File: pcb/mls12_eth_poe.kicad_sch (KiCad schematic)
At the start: 24 parts

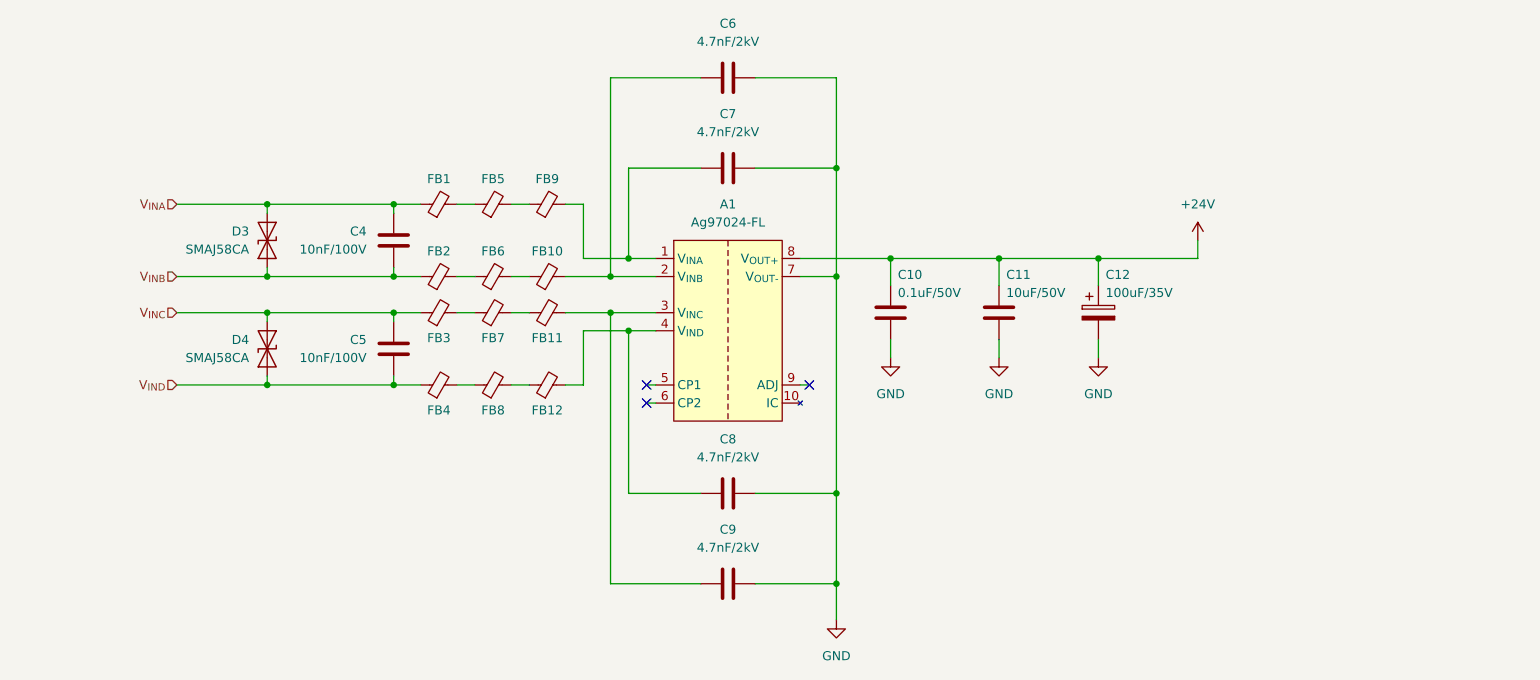
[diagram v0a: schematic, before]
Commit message: Update to 25W PoE+ module, 2 outputs
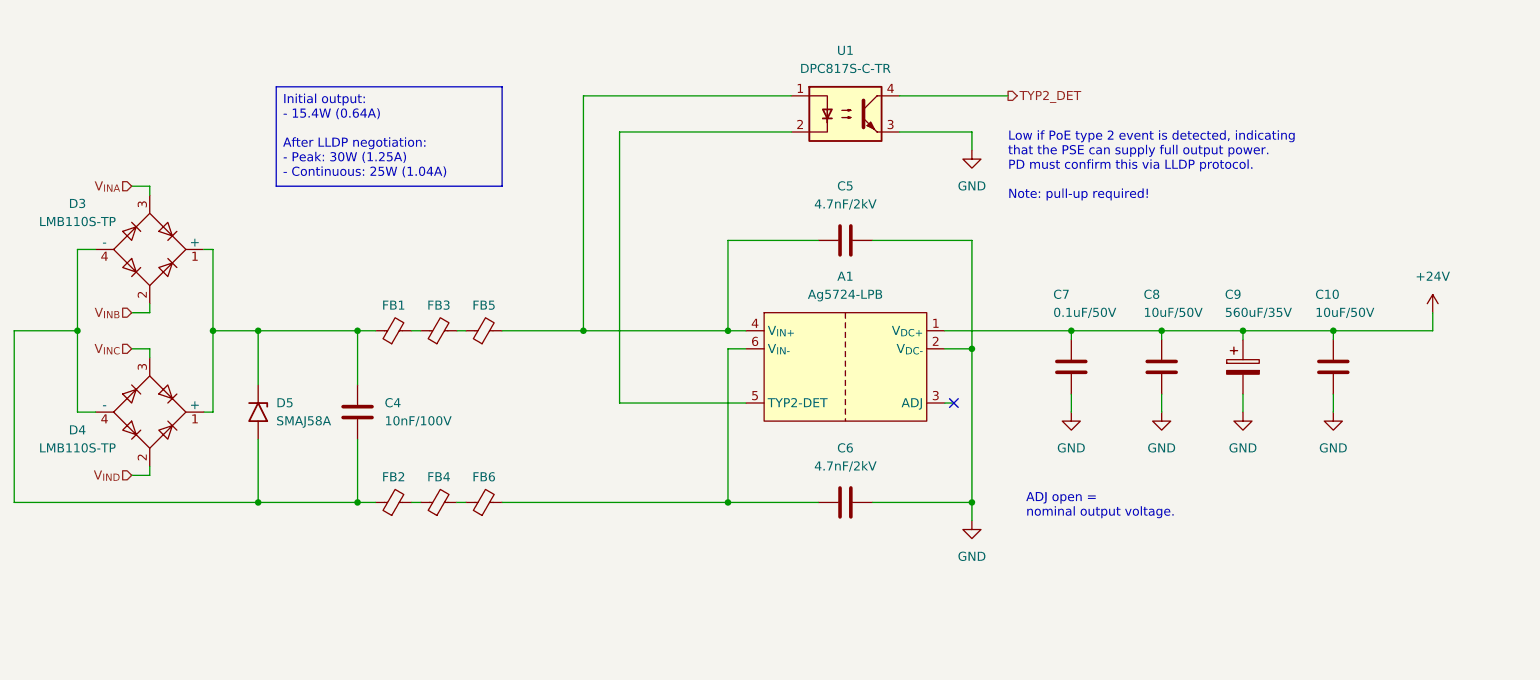
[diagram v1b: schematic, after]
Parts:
- removed A1: Ag97024-FL, mls12:Ag97024-FL, symbol mls12:Ag97024-FL
- removed C11: 10uF/50V, Capacitor_SMD:C_1206_3216Metric, symbol Device:C
- removed C12: 100uF/35V, Capacitor_SMD:CP_Elec_6.3x5.9, symbol Device:C_Polarized
- removed C9: 4.7nF/2kV, Capacitor_SMD:C_1210_3225Metric, symbol Device:C
- removed D3, D4: SMAJ58CA, Diode_SMD:D_SMA, symbol Diode:SMAJ58CA
- removed FB10, FB11, FB12, FB7, FB8, FB9: FerriteBead_Small, Inductor_SMD:L_0805_2012Metric, symbol Device:FerriteBead_Small
- added A1: Ag5724-LPB, mls12:Ag5724-LPB, symbol mls12:Ag5724-LPB
- added C9: 560uF/35V, Capacitor_SMD:CP_Elec_10x10.5, symbol Device:C_Polarized
- added D3, D4: LMB110S-TP, mls12:LMB110S-TP, symbol mls12:LMB110S-TP
- added D5: SMAJ58A, Diode_SMD:D_SMA, symbol Diode:SMAJ58A
- added U1: DPC817S-C-TR, mls12:DPC817S-C-TR, symbol Isolator:Optocoupler_DC_PhotoNPN_AKEC
- C10: value 0.1uF/50V -> 10uF/50V; footprint Capacitor_SMD:C_0603_1608Metric -> Capacitor_SMD:C_1206_3216Metric; MF Kemet -> Walsin; MPN C0603C104M5RACAUTO -> 1206X106K500CT
- C5: value 10nF/100V -> 4.7nF/2kV; footprint Capacitor_SMD:C_0603_1608Metric -> Capacitor_SMD:C_1210_3225Metric; MF TDK -> Walsin; MPN CGA3E2X7R2A103K080AA -> 1210B472K202CT
- C7: value 4.7nF/2kV -> 0.1uF/50V; footprint Capacitor_SMD:C_1210_3225Metric -> Capacitor_SMD:C_0603_1608Metric; MF Walsin -> Kemet; MPN 1210B472K202CT -> C0603C104M5RACAUTO
- C8: value 4.7nF/2kV -> 10uF/50V; footprint Capacitor_SMD:C_1210_3225Metric -> Capacitor_SMD:C_1206_3216Metric; MPN 1210B472K202CT -> 1206X106K500CT
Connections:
- net +24V: now also C7.1, C8.1, A1.1 (V_{DC+}), C9.1
- net GND: now also C5.2, A1.2 (V_{DC-}), C9.2, U1.3
- net V_{INA}: now also D3.3; no longer C4.1, FB1.1
- net V_{INB}: now also D3.2; no longer C4.2, FB2.1
- net V_{INC}: now also D4.3; no longer C5.1, FB3.1
- net V_{IND}: now also D4.2; no longer C5.2, FB4.1
- net at FB5.1: now also FB3.2; no longer FB1.2
- net at C6.1: now also FB6.2, A1.6 (V_{IN-})
- net at FB6.1: now also FB4.2; no longer FB2.2
- net at FB5.2: now also C5.1, A1.4 (V_{IN+}), U1.1
- new net: C4.1, D3.1 (+), D4.1 (+), D5.1 (A1), FB1.1
- new net: C4.2, D3.4 (-), D4.4 (-), D5.2 (A2), FB2.1
- new net: FB2.2, FB4.1
- new net: A1.5 (TYP2-DET), U1.2
- new net: FB1.2, FB3.1
- new net TYP2_DET: U1.4
- no-connect marks 3 -> 1
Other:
- note added: "ADJ open = nominal output voltage."
- note added: "Low if PoE type 2 event is detected, indicating that the PSE can supply full output power. PD must confirm this via LLDP protocol. Note: pull-up required!"
- company: (none) -> Quomodo BV

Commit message: Add test points
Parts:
- added JP1: SolderJumper_2_Bridged, Jumper:SolderJumper-2_P1.3mm_Bridged_RoundedPad1.0x1.5mm, symbol Jumper:SolderJumper_2_Bridged
- added TP1, TP33, TP6, TP8: TestPoint, TestPoint:TestPoint_Pad_1.5x1.5mm, symbol Connector:TestPoint
- added TP4, TP5, TP7: TestPoint, TestPoint:TestPoint_Pad_D1.5mm, symbol Connector:TestPoint
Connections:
- net +24V: now also JP1.1 (A), JP1.2 (B)
- net GND: now also TP1.1, TP33.1, TP8.1
- net TYP2_DET: now also TP7.1
- net at A1.4 (V_{IN+}), C5.1, FB5.2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: now also TP4.1
- net at A1.6 (V_{IN-}), C6.1, FB6.2: now also TP5.1
- new net GNDPWR: TP6.1
